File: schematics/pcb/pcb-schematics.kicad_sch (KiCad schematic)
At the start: 60 parts, among them J1 Micro_SD_Card, M1 Stepper_Motor_bipolar, M2 Stepper_Motor_bipolar, U1 LM386, U2 MCP4901, U3 L6208D, U4 L6208D, U5 TLV62568DBV

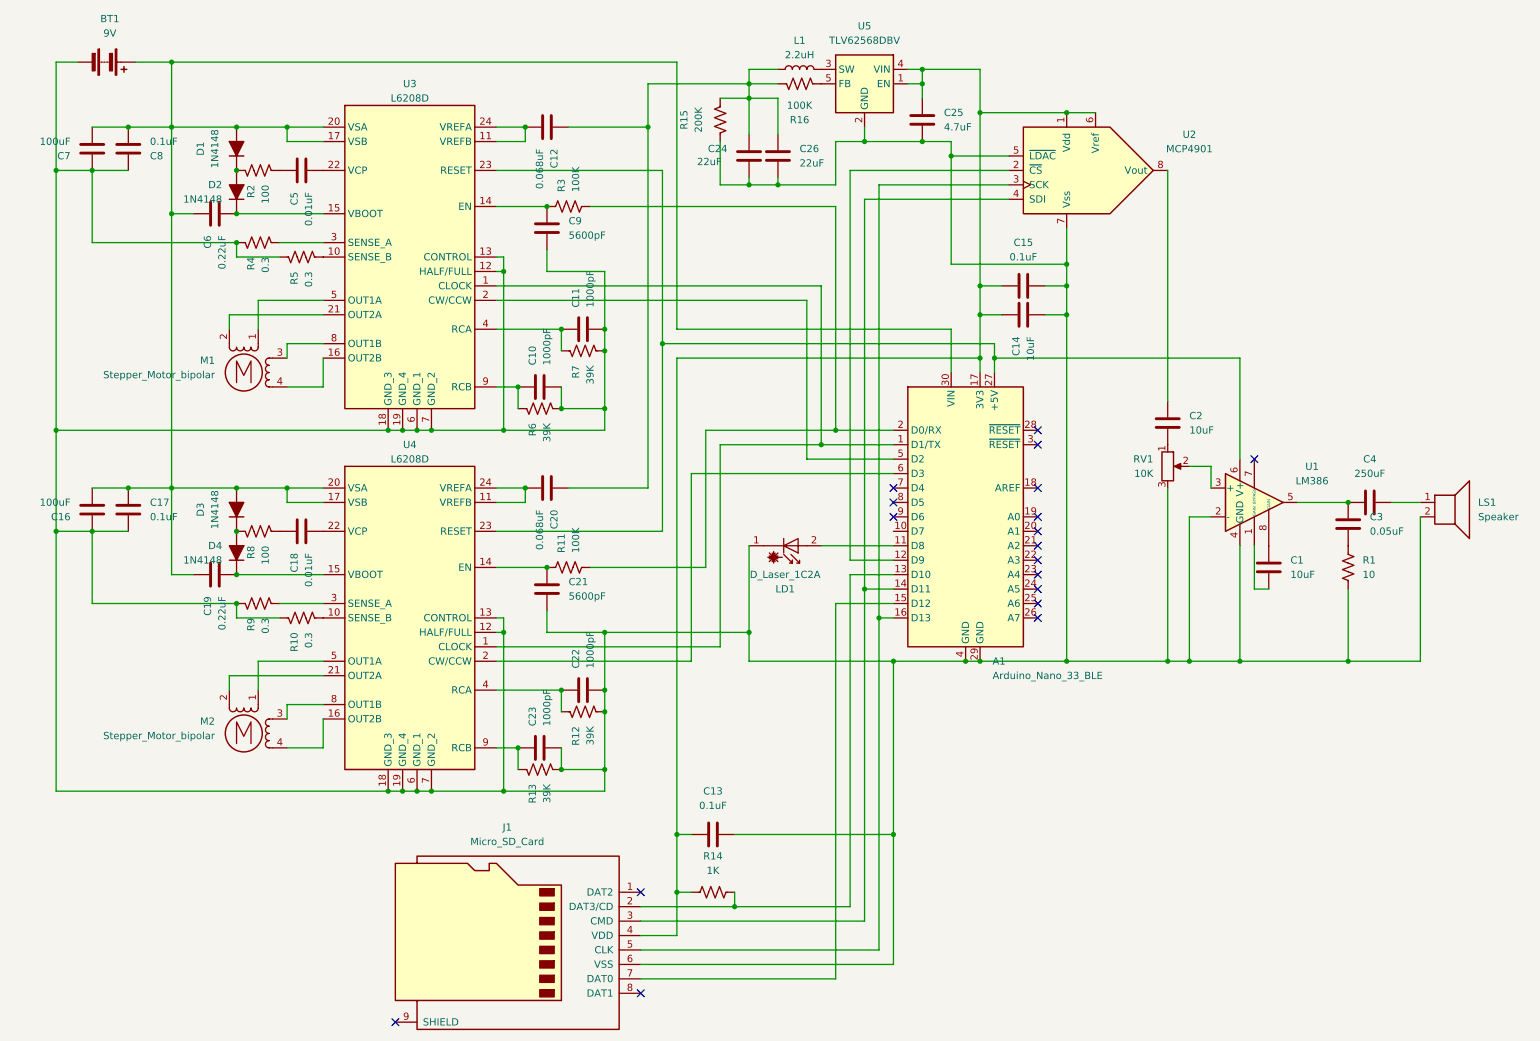
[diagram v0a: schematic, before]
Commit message: schematic and driver rewrite
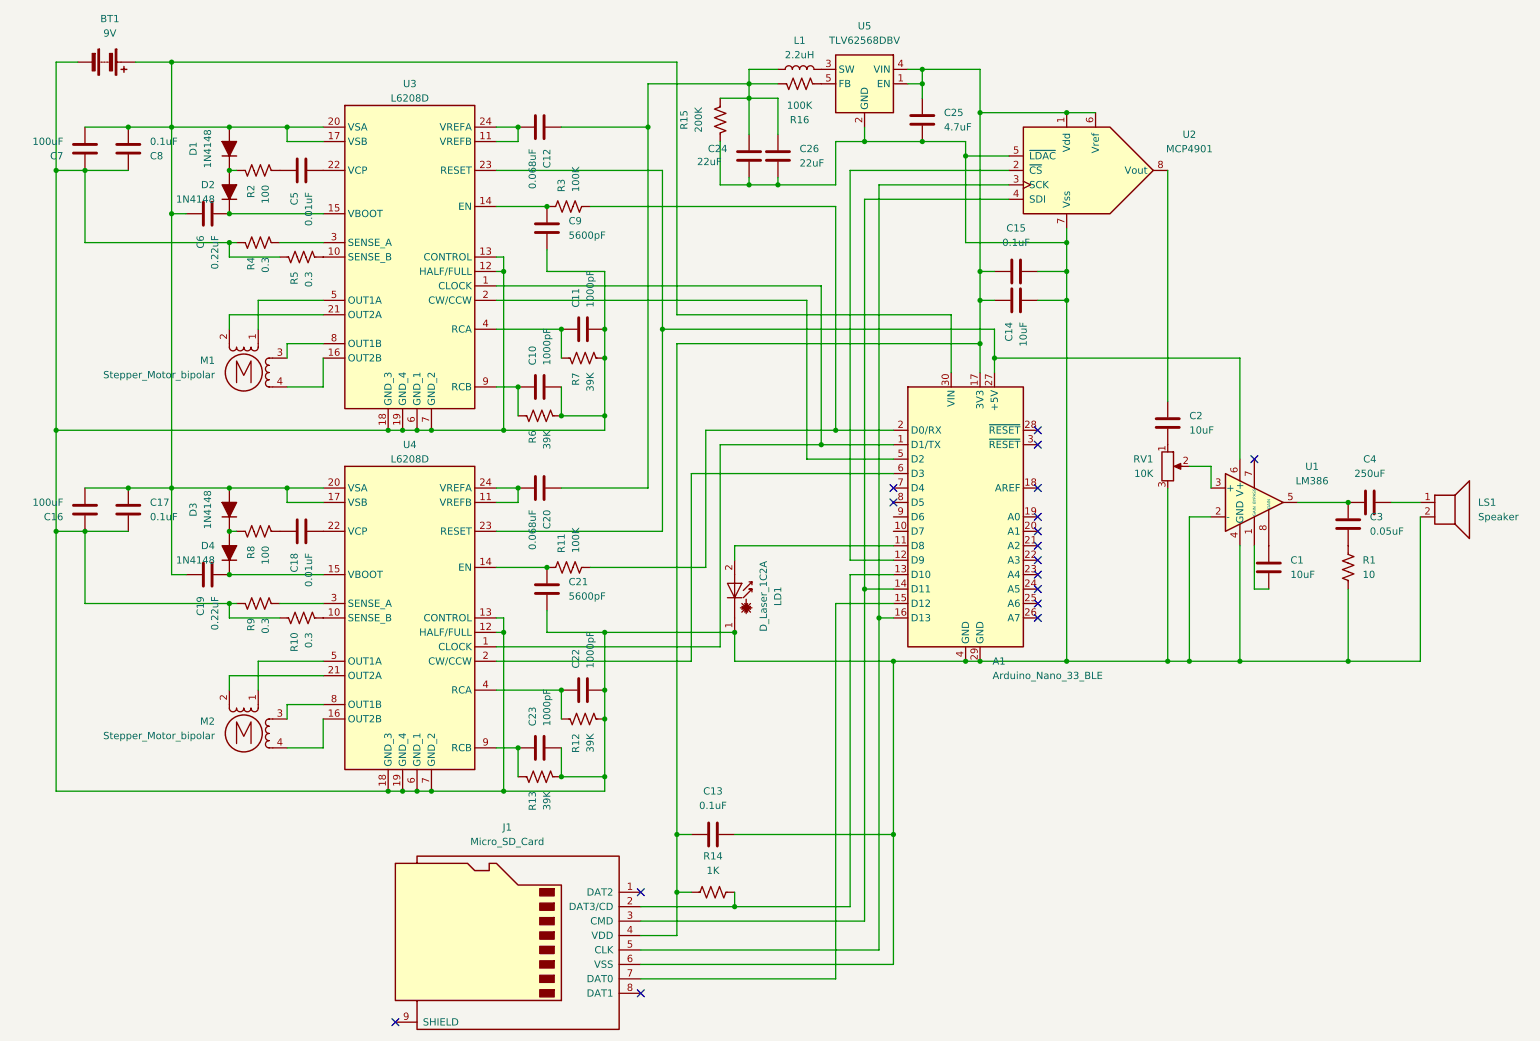
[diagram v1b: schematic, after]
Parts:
- BT1: footprint (none) -> Connector:JWT_A3963_1x02_P3.96mm_Vertical
- C24, C26: footprint (none) -> Capacitor_SMD:C_1206_3216Metric
- C25: footprint (none) -> Capacitor_SMD:C_0603_1608Metric
- L1: footprint (none) -> Inductor_SMD:L_1812_4532Metric
- R15, R16: footprint (none) -> Resistor_SMD:R_1206_3216Metric
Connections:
- no-connect marks 18 -> 17
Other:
- moved on the sheet: C12, C14, C15, C16, C19, C20, C6, C7, D1, D2, D3, D4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

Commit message: more frame rewriting
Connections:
- net at C12.1, C20.1, C24.2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: no longer R15.2
- net at R16.1, U5.5 (FB): now also R15.2
- net at A1.27 (+5V), U1.6 (V+): no longer U3.23 (RESET), U4.23 (RESET)
- net at A1.7 (D4): now also U3.23 (RESET), U4.23 (RESET)
- no-connect marks 17 -> 15
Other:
- moved on the sheet: C24, C26, R15, R16

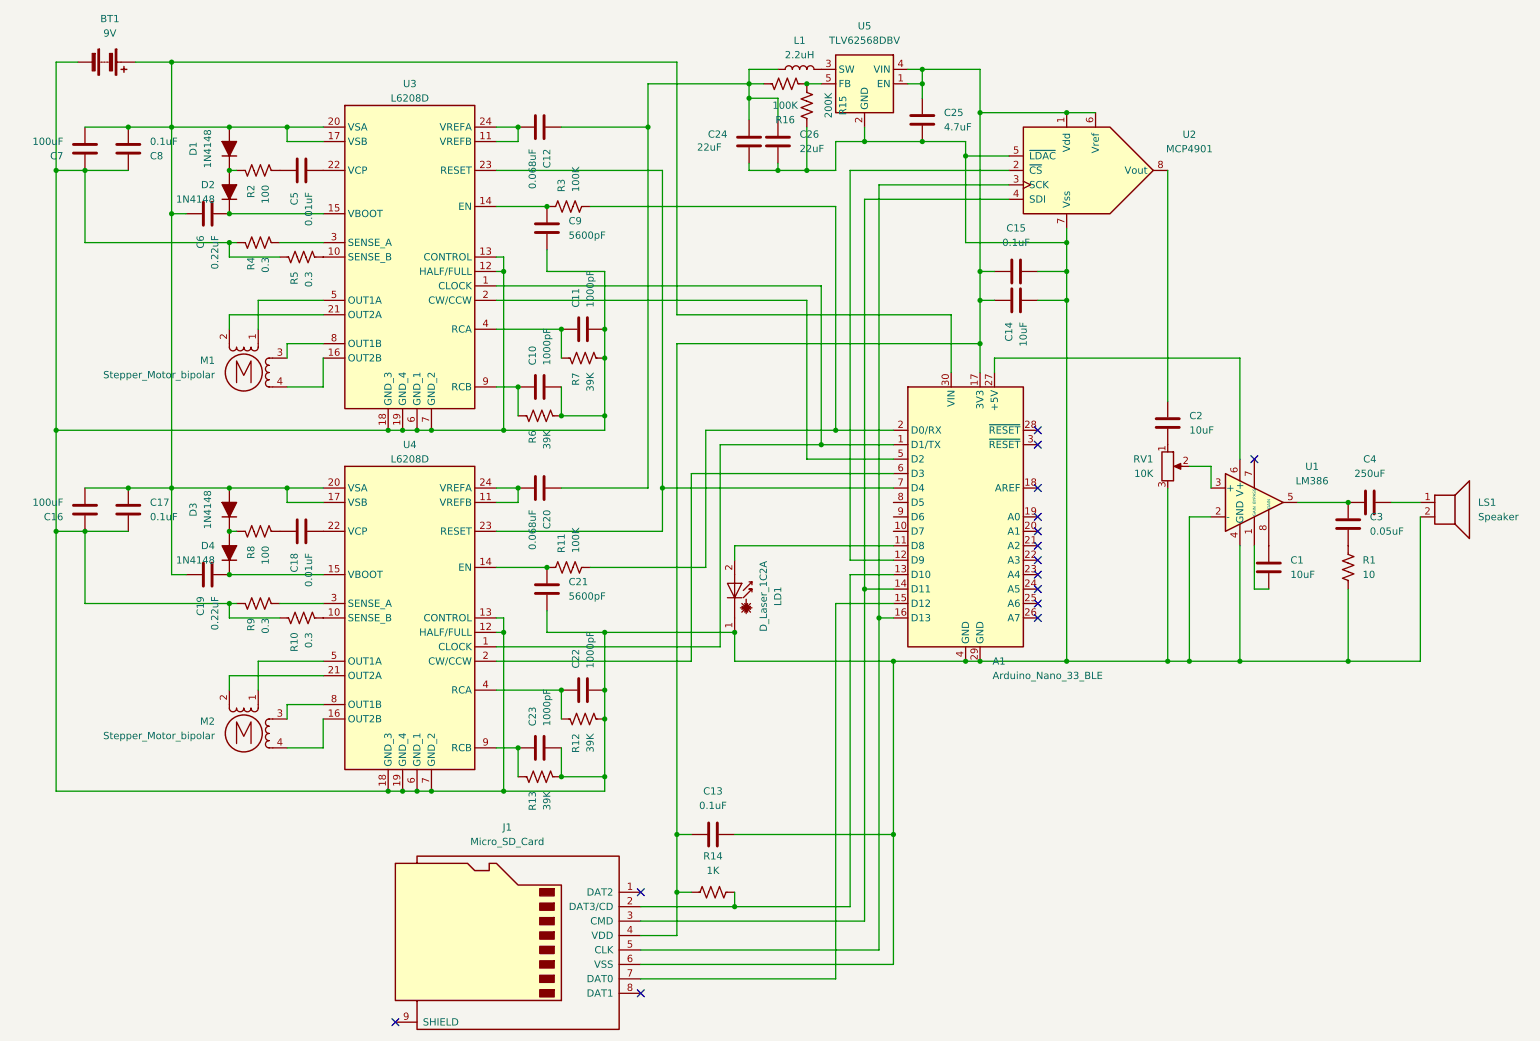
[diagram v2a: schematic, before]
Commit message: KiCad schematics at manufacture
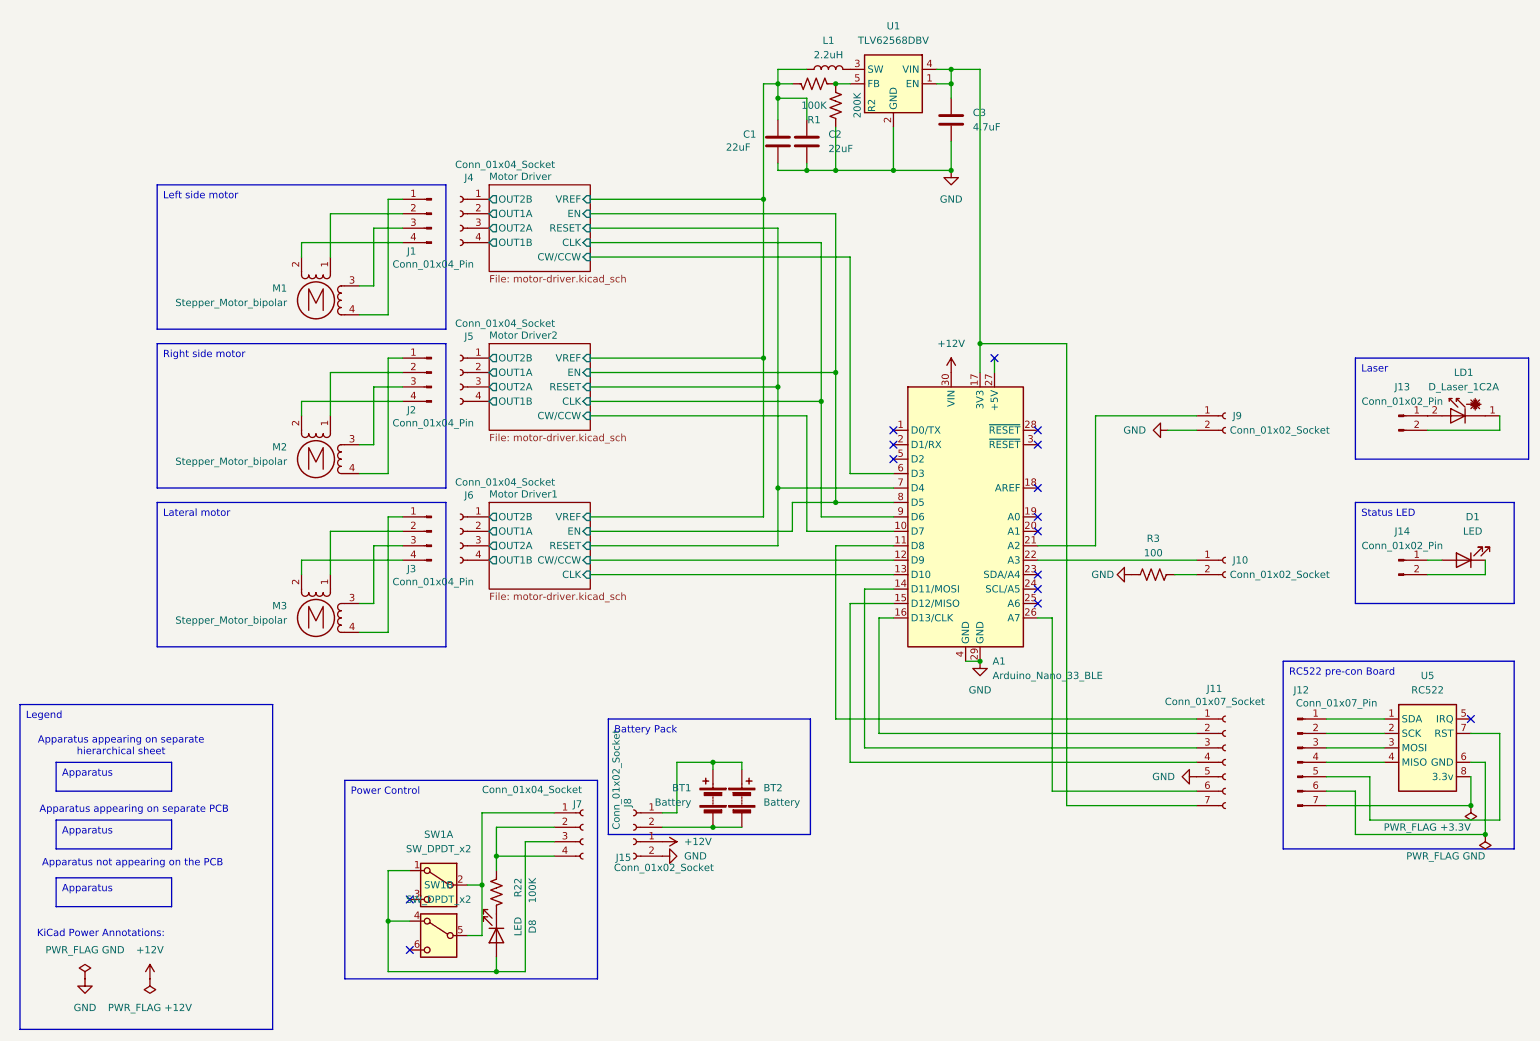
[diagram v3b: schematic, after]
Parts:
- removed A1: Arduino_Nano_33_BLE, Module:Arduino_Nano, symbol MCU_Module:Arduino_Nano_v2.x
- removed C1, C14, C2: 10uF, Capacitor_SMD:C_0201_0603Metric_Pad0.64x0.40mm_HandSolder, symbol Device:C
- removed C10, C11, C22, C23: 1000pF, Capacitor_SMD:C_0402_1005Metric, symbol Device:C
- removed C12, C20: 0.068uF, Capacitor_SMD:C_0402_1005Metric, symbol Device:C
- removed C13: 0.1uF, Capacitor_SMD:C_0201_0603Metric, symbol Device:C
- removed C15, C17, C8: 0.1uF, Capacitor_SMD:C_0201_0603Metric_Pad0.64x0.40mm_HandSolder, symbol Device:C
- removed C16, C7: 100uF, Capacitor_SMD:C_1210_3225Metric, symbol Device:C
- removed C18, C5: 0.01uF, Capacitor_SMD:C_0201_0603Metric, symbol Device:C
- removed C19, C6: 0.22uF, Capacitor_SMD:C_0201_0603Metric, symbol Device:C
- removed C21, C9: 5600pF, Capacitor_SMD:C_0402_1005Metric, symbol Device:C
- removed C3: 0.05uF, Capacitor_SMD:C_0805_2012Metric, symbol Device:C
- removed C4: 250uF, Capacitor_THT:CP_Axial_L34.5mm_D20.0mm_P41.00mm_Horizontal, symbol Device:C
- removed D1, D2, D3, D4: 1N4148, Diode_SMD:D_SOD-523, symbol Device:D_Filled
- removed J1: Micro_SD_Card, Connector_PinSocket_2.54mm:PinSocket_1x06_P2.54mm_Vertical, symbol Connector:Micro_SD_Card
- removed LS1: Speaker, Connector_Molex:Molex_Pico-Clasp_501331-0207_1x02-1MP_P1.00mm_Vertical, symbol Device:Speaker
- removed R1: 10, Resistor_SMD:R_1812_4532Metric, symbol Device:R_US
- removed R10, R4, R5, R9: 0.3, Resistor_SMD:R_0805_2012Metric, symbol Device:R_US
- removed R11: 100K, Resistor_SMD:R_1206_3216Metric, symbol Device:R_US
- removed R12, R13, R6, R7: 39K, Resistor_SMD:R_0612_1632Metric, symbol Device:R_US
- removed R14: 1K, Resistor_SMD:R_1020_2550Metric, symbol Device:R_US
- removed R2, R8: 100, Resistor_SMD:R_1206_3216Metric, symbol Device:R_US
- removed RV1: 10K, Connector_Molex:Molex_Pico-Clasp_202396-0307_1x03-1MP_P1.00mm_Horizontal, symbol Device:R_Potentiometer
- removed U1: LM386, Package_SO:SOIC-8-N7_3.9x4.9mm_P1.27mm, symbol Amplifier_Audio:LM386
- removed U2: MCP4901, Package_SO:SOIC-8-N7_3.9x4.9mm_P1.27mm, symbol Analog_DAC:MCP4901
- removed U3, U4: L6208D, Package_SO:ST_PowerSSO-24_SlugUp, symbol Driver_Motor:L6208D
- added A1: Arduino_Nano_33_BLE, Module:Arduino_Nano, symbol MCU_Module:Arduino_Nano_33_BLE
- added BT2: Battery, PersonalLibraries:Battery_clip-MPD_BHA23APC, symbol Device:Battery
- added D1: LED, symbol Device:LED
- added D8: LED, LED_THT:LED_D3.0mm, symbol Device:LED
- added J1, J2, J3: Conn_01x04_Pin, symbol Connector:Conn_01x04_Pin
- added J10, J15, J8, J9: Conn_01x02_Socket, Connector_Molex:Molex_PicoBlade_53261-0271_1x02-1MP_P1.25mm_Horizontal, symbol Connector:Conn_01x02_Socket
- added J11: Conn_01x07_Socket, Connector_Molex:Molex_PicoBlade_53261-0771_1x07-1MP_P1.25mm_Horizontal, symbol Connector:Conn_01x07_Socket
- added J12: Conn_01x07_Pin, symbol Connector:Conn_01x07_Pin
- added J13, J14: Conn_01x02_Pin, symbol Connector:Conn_01x02_Pin
- added J4, J5, J6, J7: Conn_01x04_Socket, Connector_Molex:Molex_PicoBlade_53261-0471_1x04-1MP_P1.25mm_Horizontal, symbol Connector:Conn_01x04_Socket
- added M3: Stepper_Motor_bipolar, Connector_Molex:Molex_Pico-Clasp_501331-0407_1x04-1MP_P1.00mm_Vertical, symbol Motor:Stepper_Motor_bipolar
- added R22: 100K, Resistor_SMD:R_1206_3216Metric, symbol Device:R_US
- added SW1: SW_DPDT_x2, PersonalLibraries:SW-Slide_Diptronics-LSSA22, symbol Switch:SW_DPDT_x2
- added U5: RC522, Connector_Molex:Molex_Pico-Clasp_202396-0807_1x08-1MP_P1.00mm_Horizontal, symbol RF_RFID:RC522
- BT1: value 9V -> Battery; footprint Connector:JWT_A3963_1x02_P3.96mm_Vertical -> PersonalLibraries:Battery_clip-MPD_BHA23APC
- R3: value 100K -> 100
- renumbered C24 to C1, C26 to C2, C25 to C3, R16 to R1, R15 to R2, U5 to U1
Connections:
- net at BT1.1 (+): now also BT2.1 (+), J8.1 (Pin_1)
- net GND: now reaches C1.1, C2.1, C3.2, R2.1, U1.2 (GND)
- net GND: now also R3.2, A1.29 (GND), A1.4 (GND), J11.5 (Pin_5), J15.2 (Pin_2), J9.2 (Pin_2); no longer BT1.2 (-), LD1.1 (K)
- net Motor Driver/VREF: now reaches C1.2, C2.2, L1.1, R1.2
- net at C3.1, U1.1 (EN), U1.4 (VIN): now also A1.17 (3V3), J11.7 (Pin_7)
- net at LD1.2 (A): now also J13.1 (Pin_1)
- net at R3.1: now also J10.2 (Pin_2)
- net at M1.4: now also J1.1 (Pin_1)
- net at M1.2 (-): now also J1.4 (Pin_4)
- net at M1.1: now also J1.2 (Pin_2)
- net at M1.3: now also J1.3 (Pin_3)
- net at M2.4: now also J2.1 (Pin_1)
- net at M2.2 (-): now also J2.4 (Pin_4)
- net at M2.1: now also J2.2 (Pin_2)
- net at M2.3: now also J2.3 (Pin_3)
- new net: J12.1 (Pin_1), U5.1 (SDA)
- new net: J12.2 (Pin_2), U5.2 (SCK)
- new net: J12.3 (Pin_3), U5.3 (MOSI)
- new net: J12.4 (Pin_4), U5.4 (MISO)
- new net: J12.6 (Pin_6), U5.6 (GND)
- new net: J12.5 (Pin_5), U5.7 (RST)
- new net: J12.7 (Pin_7), U5.8 (3.3v)
- new net: A1.21 (A2), J9.1 (Pin_1)
- new net: BT1.2 (-), BT2.2 (-), J8.2 (Pin_2)
- new net: J7.1 (Pin_1), SW1.2 (B), SW1.5 (B)
- new net: J7.2 (Pin_2), J7.4 (Pin_4), R22.1
- new net: D8.2 (A), J7.3 (Pin_3), SW1.1 (A), SW1.4 (A)
- new net: J3.2 (Pin_2), M3.1
- new net: J3.4 (Pin_4), M3.2 (-)
- new net: J3.3 (Pin_3), M3.3
- new net: J3.1 (Pin_1), M3.4
- new net: A1.11 (D8), J11.1 (Pin_1)
- new net: A1.16 (D13/CLK), J11.2 (Pin_2)
- new net: A1.14 (D11/MOSI), J11.3 (Pin_3)
- new net: A1.15 (D12/MISO), J11.4 (Pin_4)
- new net: A1.26 (A7), J11.6 (Pin_6)
- new net: D8.1 (K), R22.2
- new net: A1.22 (A3), J10.1 (Pin_1)
- new net: J13.2 (Pin_2), LD1.1 (K)
- new net: D1.2 (A), J14.1 (Pin_1)
- new net: D1.1 (K), J14.2 (Pin_2)
- new net +12V: A1.30 (VIN), J15.1 (Pin_1)
- new net Motor Driver/CLK: A1.9 (D6)
- new net Motor Driver/CW/CCW: A1.6 (D3)
- new net Motor Driver/EN: A1.8 (D5)
- new net Motor Driver/OUT1A: J4.2 (Pin_2)
- new net Motor Driver/OUT1B: J4.4 (Pin_4)
- new net Motor Driver/OUT2A: J4.3 (Pin_3)
- new net Motor Driver/OUT2B: J4.1 (Pin_1)
- new net Motor Driver/RESET: A1.7 (D4)
- new net Motor Driver1/CLK: A1.13 (D10)
- new net Motor Driver1/CW/CCW: A1.12 (D9)
- new net Motor Driver1/OUT1A: J6.2 (Pin_2)
- new net Motor Driver1/OUT1B: J6.4 (Pin_4)
- new net Motor Driver1/OUT2A: J6.3 (Pin_3)
- new net Motor Driver1/OUT2B: J6.1 (Pin_1)
- new net Motor Driver2/CW/CCW: A1.10 (D7)
- new net Motor Driver2/OUT1A: J5.2 (Pin_2)
- new net Motor Driver2/OUT1B: J5.4 (Pin_4)
- new net Motor Driver2/OUT2A: J5.3 (Pin_3)
- new net Motor Driver2/OUT2B: J5.1 (Pin_1)
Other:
- added sheet Motor Driver (motor-driver.kicad_sch)
- added sheet Motor Driver1 (motor-driver.kicad_sch)
- added sheet Motor Driver2 (motor-driver.kicad_sch)
- note added: "Apparatus appearing on separate PCB"
- note added: "Apparatus appearing on separate hierarchical sheet"
- note added: "Apparatus not appearing on the PCB"
- note added: "KiCad Power Annotations:"
- title: Twonky Internal Schematic -> Device Schematic
- moved on the sheet: C1, C2, C3, L1, R1, R2, U1
